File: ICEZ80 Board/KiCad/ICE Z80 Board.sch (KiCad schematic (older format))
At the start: 2 parts, among them M1 ICE-Z80, U1 Z80CPU

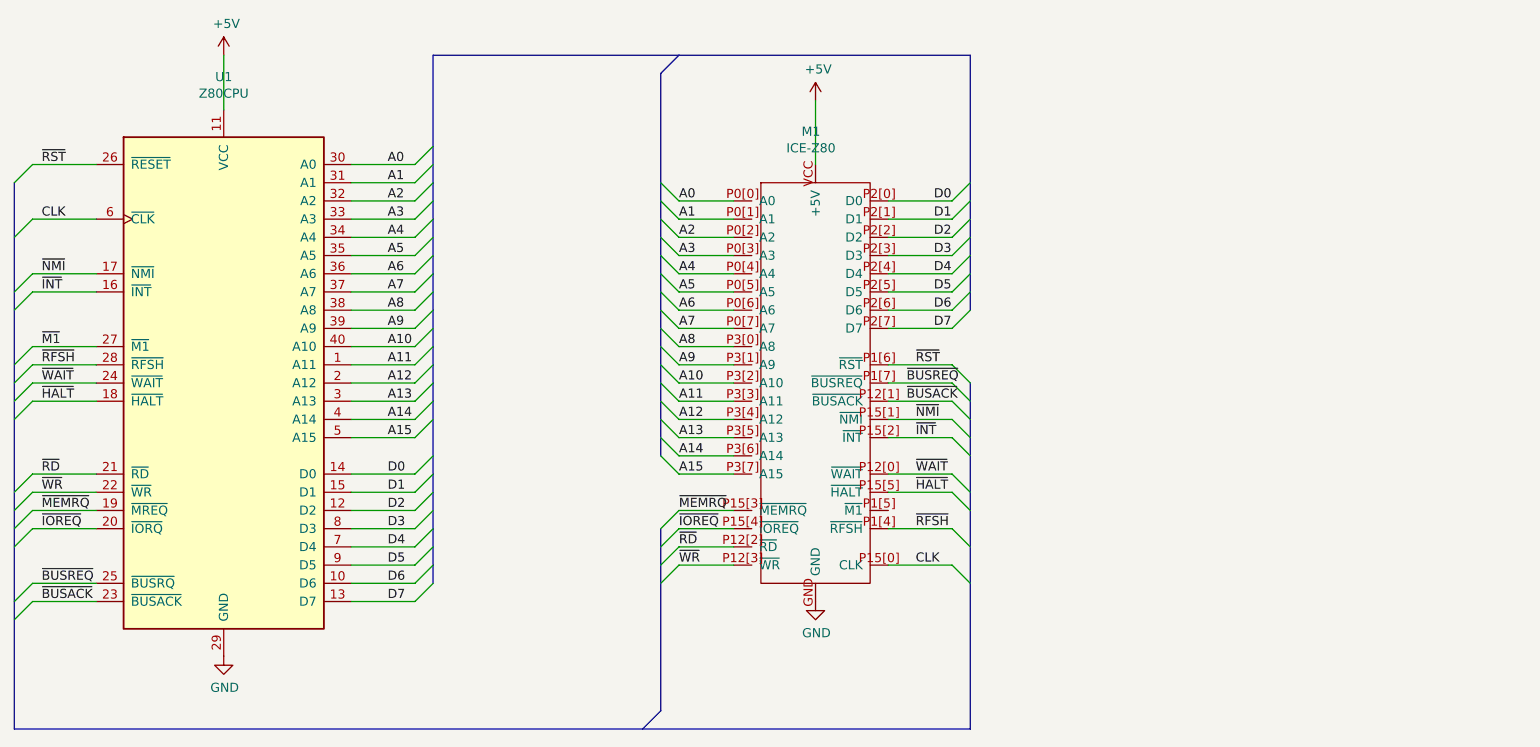
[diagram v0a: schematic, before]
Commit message: add header and power option
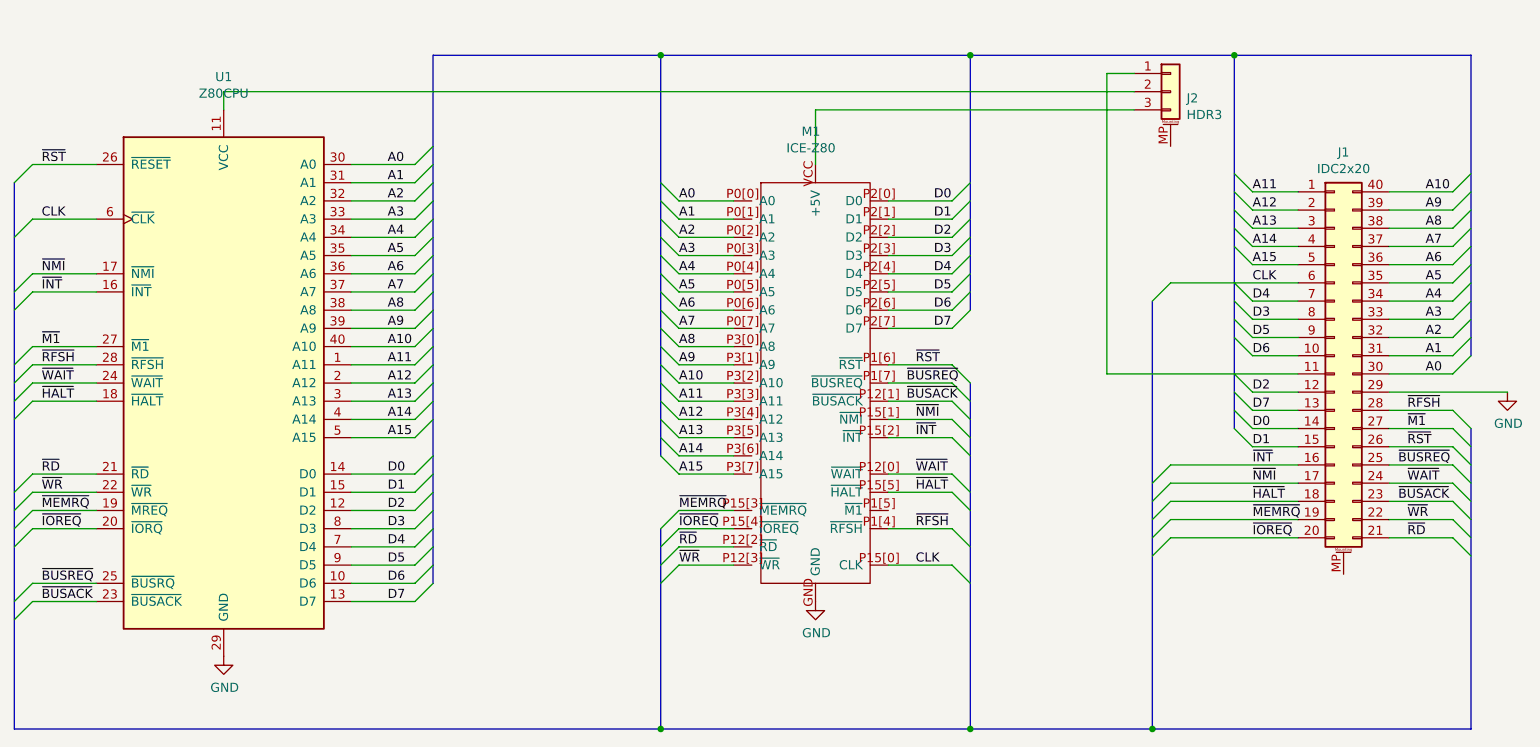
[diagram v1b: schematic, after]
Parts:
- added J1: IDC2x20, symbol Connector_Generic_MountingPin:Conn_02x20_Counter_Clockwise_MountingPin
- added J2: HDR3, symbol Connector_Generic_MountingPin:Conn_01x03_MountingPin
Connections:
- net A0: now also J1.30 (Pin_30)
- net A1: now also J1.31 (Pin_31)
- net A10: now also J1.40 (Pin_40)
- net A11: now also J1.1 (Pin_1)
- net A12: now also J1.2 (Pin_2)
- net A13: now also J1.3 (Pin_3)
- net A14: now also J1.4 (Pin_4)
- net A15: now also J1.5 (Pin_5)
- net A2: now also J1.32 (Pin_32)
- net A3: now also J1.33 (Pin_33)
- net A4: now also J1.34 (Pin_34)
- net A5: now also J1.35 (Pin_35)
- net A6: now also J1.36 (Pin_36)
- net A7: now also J1.37 (Pin_37)
- net A8: now also J1.38 (Pin_38)
- net A9: now also J1.39 (Pin_39)
- net CLK: now also J1.6 (Pin_6)
- net D0: now also J1.14 (Pin_14)
- net D1: now also J1.15 (Pin_15)
- net D2: now also J1.12 (Pin_12)
- net D3: now also J1.8 (Pin_8)
- net D4: now also J1.7 (Pin_7)
- net D5: now also J1.9 (Pin_9)
- net D6: now also J1.10 (Pin_10)
- net D7: now also J1.13 (Pin_13)
- net GND: now also J1.29 (Pin_29)
- net ~BUSACK: now also J1.23 (Pin_23)
- net ~BUSREQ: now also J1.25 (Pin_25)
- net ~HALT: now also J1.18 (Pin_18)
- net ~INT: now also J1.16 (Pin_16)
- net ~IOREQ: now also J1.20 (Pin_20)
- net ~M1: now also J1.27 (Pin_27)
- net ~MEMRQ: now also J1.19 (Pin_19)
- net ~NMI: now also J1.17 (Pin_17)
- net ~RD: now also J1.21 (Pin_21)
- net ~RFSH: now also J1.28 (Pin_28)
- net ~RST: now also J1.26 (Pin_26)
- net ~WAIT: now also J1.24 (Pin_24)
- net ~WR: now also J1.22 (Pin_22)
- net +5V: no longer names the net of U1.11 (VCC)
- net +5V: now also J2.2 (Pin_2); no longer M1.VCC (+5V)
- new net: J2.3 (Pin_3), M1.VCC (+5V)
- new net: J1.11 (Pin_11), J2.1 (Pin_1)

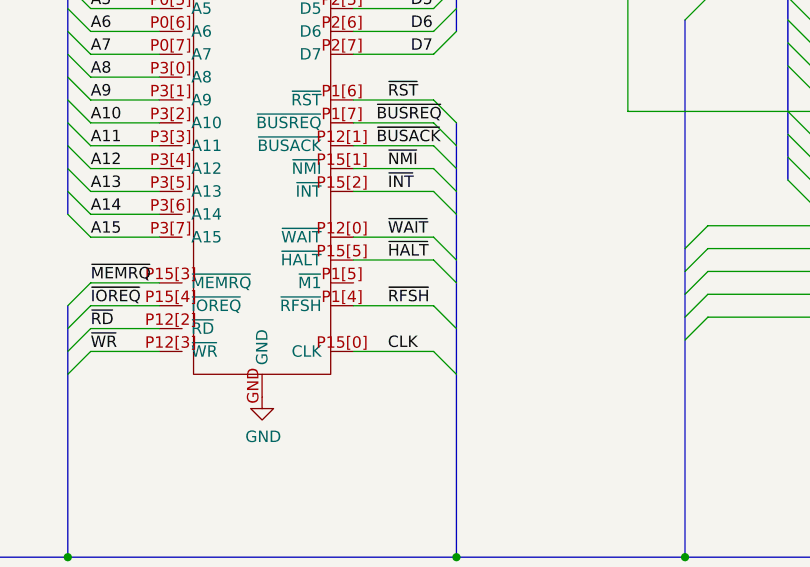
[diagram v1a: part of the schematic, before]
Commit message: Final pin assignment ICE Z80
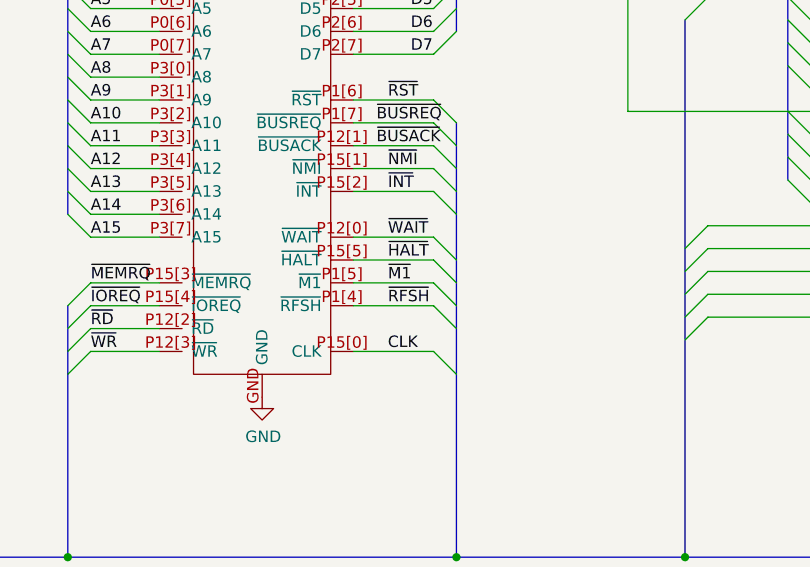
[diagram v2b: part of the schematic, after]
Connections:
- net ~M1: now also M1.P1[5] (~M1)
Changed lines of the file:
@@
-	1    0    0    -1
-$EndComp
-$Comp
-L ICEZ80:ICE-Z80 M1
-U 1 1 5D7E8879
-P 6300 1850
-F 0 "M1" H 6275 2231 50  0000 C CNN
-F 1 "ICE-Z80" H 6275 2140 50  0000 C CNN
-F 2 "" H 6300 1850 50  0001 C CNN
-F 3 "" H 6300 1850 50  0001 C CNN
-	1    6300 1850
 	1    0    0    -1
 $EndComp
@@
 Wire Bus Line
 	5450 4750 7150 4750
+$Comp
+L ICEZ80:ICE-Z80 M1
+U 1 1 5D837DF8
+P 6300 1850
+F 0 "M1" H 6275 2231 50  0000 C CNN
+F 1 "ICE-Z80" H 6275 2140 50  0000 C CNN
+F 2 "" H 6300 1850 50  0001 C CNN
+F 3 "" H 6300 1850 50  0001 C CNN
+	1    6300 1850
+	1    0    0    -1
+$EndComp
+Wire Wire Line
+	6700 3550 7050 3550
 Wire Wire Line
 	7900 2800 8950 2800
@@
 Wire Bus Line
 	4200 1050 4200 3950
+Entry Wire Line
+	7050 3550 7150 3650
+Text Label 6850 3550 0    50   ~ 0
+~M1
 $EndSCHEMATC

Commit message: Board fixes
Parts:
- J1: footprint (none) -> Connector_IDC:IDC-Header_2x20_P2.54mm_Vertical
- J2: footprint (none) -> Connector_PinHeader_2.54mm:PinHeader_1x03_P2.54mm_Vertical
- M1: footprint (none) -> ProjectFootprints:DIP-52_485_ELL
- U1: footprint (none) -> Package_DIP:DIP-40_W15.24mm_LongPads
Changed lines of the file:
@@
 F 0 "U1" H 3050 4531 50  0000 C CNN
 F 1 "Z80CPU" H 3050 4440 50  0000 C CNN
-F 2 "" H 3050 3250 50  0001 C CNN
+F 2 "Package_DIP:DIP-40_W15.24mm_LongPads" H 3050 3250 50  0001 C CNN
 F 3 "www.zilog.com/manage_directlink.php?filepath=docs/z80/um0080" H 3050 3250 50  0001 C CNN
 	1    3050 2850
@@
 	5850 3850 5550 3850
 Wire Wire Line
-	6700 1850 7050 1850
-Wire Wire Line
-	6700 1950 7050 1950
-Wire Wire Line
-	6700 2050 7050 2050
-Wire Wire Line
-	6700 2150 7050 2150
-Wire Wire Line
-	6700 2250 7050 2250
-Wire Wire Line
-	6700 2350 7050 2350
-Wire Wire Line
-	6700 2450 7050 2450
-Wire Wire Line
-	6700 2550 7050 2550
-Wire Wire Line
-	6700 2750 7050 2750
-Wire Wire Line
-	6700 2850 7050 2850
-Wire Wire Line
-	6700 2950 7050 2950
-Wire Wire Line
-	6700 3050 7050 3050
-Wire Wire Line
-	6700 3150 7050 3150
-Wire Wire Line
-	6700 3350 7050 3350
-Wire Wire Line
 	6700 3450 7050 3450
-Wire Wire Line
-	6700 3650 7050 3650
-Wire Wire Line
-	6700 3850 7050 3850
 Entry Wire Line
 	7050 1850 7150 1750
@@
 F 0 "J1" H 9200 3817 50  0000 C CNN
 F 1 "IDC2x20" H 9200 3726 50  0000 C CNN
-F 2 "" H 9150 2700 50  0001 C CNN
+F 2 "Connector_IDC:IDC-Header_2x20_P2.54mm_Vertical" H 9150 2700 50  0001 C CNN
 F 3 "~" H 9150 2700 50  0001 C CNN
 	1    9150 2700
@@
 F 0 "J2" H 8338 1214 50  0000 L CNN
 F 1 "HDR3" H 8338 1123 50  0000 L CNN
-F 2 "" H 8250 1250 50  0001 C CNN
+F 2 "Connector_PinHeader_2.54mm:PinHeader_1x03_P2.54mm_Vertical" H 8250 1250 50  0001 C CNN
 F 3 "~" H 8250 1250 50  0001 C CNN
 	1    8250 1250
@@
 Wire Bus Line
 	5450 4750 7150 4750
+Entry Wire Line
+	7050 3550 7150 3650
+Text Label 6850 3550 0    50   ~ 0
+~M1
+Wire Wire Line
+	6700 3350 7050 3350
+Wire Wire Line
+	6700 3150 7050 3150
+Wire Wire Line
+	6700 3050 7050 3050
+Wire Wire Line
+	6700 2950 7050 2950
+Wire Wire Line
+	6700 2850 7050 2850
+Wire Wire Line
+	6700 2750 7050 2750
+Wire Wire Line
+	6700 3650 7050 3650
+Wire Wire Line
+	6700 3550 7050 3550
+Wire Wire Line
+	6700 3850 7050 3850
+Wire Wire Line
+	6700 2550 7050 2550
+Wire Wire Line
+	6700 2450 7050 2450
+Wire Wire Line
+	6700 2350 7050 2350
+Wire Wire Line
+	6700 2250 7050 2250
+Wire Wire Line
+	6700 2150 7050 2150
+Wire Wire Line
+	6700 2050 7050 2050
+Wire Wire Line
+	6700 1950 7050 1950
+Wire Wire Line
+	6700 1850 7050 1850
 $Comp
 L ICEZ80:ICE-Z80 M1
@@
 F 0 "M1" H 6275 2231 50  0000 C CNN
 F 1 "ICE-Z80" H 6275 2140 50  0000 C CNN
-F 2 "" H 6300 1850 50  0001 C CNN
+F 2 "ProjectFootprints:DIP-52_485_ELL" H 6300 1850 50  0001 C CNN
 F 3 "" H 6300 1850 50  0001 C CNN
 	1    6300 1850
@@
 $EndComp
 Wire Wire Line
-	6700 3550 7050 3550
-Wire Wire Line
 	7900 2800 8950 2800
 Wire Wire Line
@@
 Wire Bus Line
 	4200 1050 4200 3950
-Entry Wire Line
-	7050 3550 7150 3650
-Text Label 6850 3550 0    50   ~ 0
-~M1
 $EndSCHEMATC
